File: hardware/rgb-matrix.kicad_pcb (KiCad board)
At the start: 4 copper layers, 58 x 58 mm, 138 parts, among them CON1 VEXT, P1 MATRIX_BOT, P10 PSOUTH, P11 PEAST, P12 WEST, P13 NORTH, P14 SOUTH, P15 EAST, P2 MATRIX_TOP, P3 SWD, P4 SPI3, P5 UART5, P6 VEXT, P7 USB_B, P8 PWEST, P9 PNORTH, SW1 RESET, SW2 BOOT, U1 74AC244, U2 74AC244, U3 74AC244, U4 ULN2803A, U5 STM32F405R, U6 LD3985M33R, U7 USBUF01W6, X1 8MHz

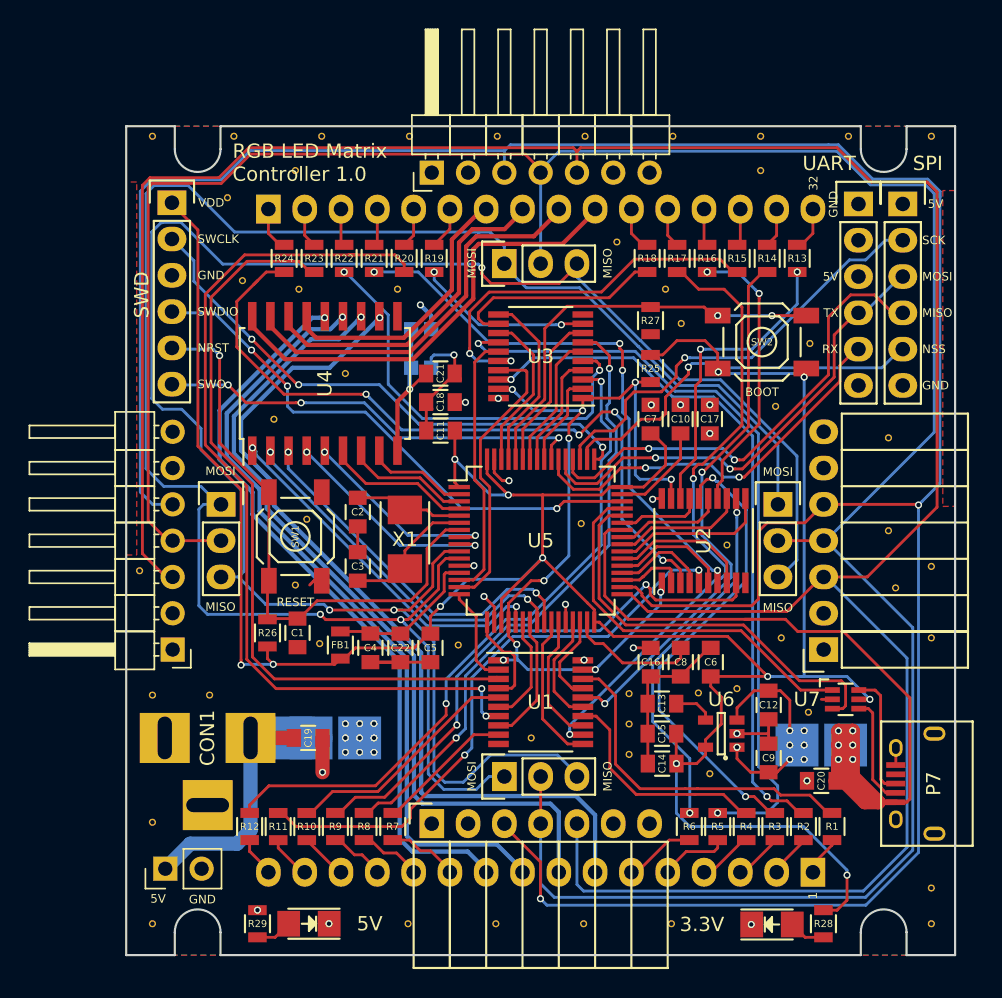
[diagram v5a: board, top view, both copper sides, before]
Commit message: Add silk: name and URL
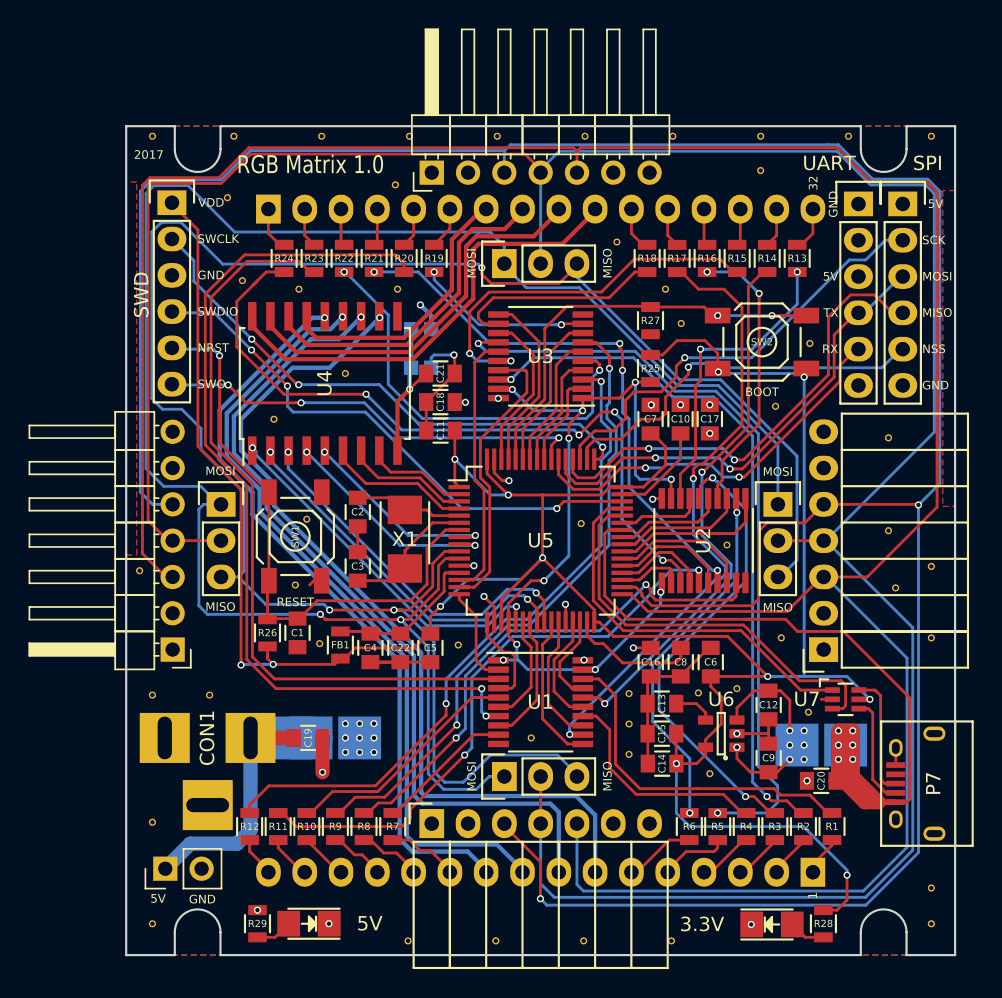
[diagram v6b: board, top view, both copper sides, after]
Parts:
- moved REF** 7.07 mm to (152.0, 76.3)
- moved REF** 1.20 mm to (152.9, 129.2)
- moved REF** 1.20 mm to (159.0, 129.2)
- moved REF** 1.20 mm to (165.2, 129.2)
- moved REF** 1.20 mm to (171.3, 129.2)
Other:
- board text added: "2017"
- board text added: "RGB Matrix 1.0"
- board text added: "https://github.com/joh/rgb-matrix"
- board text removed: "BOTTOM"
- board text removed: "RGB LED Matrix Controller 1.0"
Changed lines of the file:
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@@
     (area 133.088999 72.120999 191.239001 130.271001)
     (thickness 1.6)
-    (drawings 69)
+    (drawings 70)
     (tracks 1575)
     (zones 0)
@@
   )
   (module VIA-0.5mm (layer Top)
-    (at 152.885715 128 180)
+    (at 152.885715 129.2 180)
     (fp_text reference REF** (at 0 0.4 180) (layer F.SilkS) hide
       (effects (font (size 0.127 0.127) (thickness 0.03175)))
@@
   )
   (module VIA-0.5mm (layer Top)
-    (at 159.028572 128 180)
+    (at 159.028572 129.2 180)
     (fp_text reference REF** (at 0 0.4 180) (layer F.SilkS) hide
       (effects (font (size 0.127 0.127) (thickness 0.03175)))
@@
   )
   (module VIA-0.5mm (layer Top)
-    (at 165.171429 128 180)
+    (at 165.171429 129.2 180)
     (fp_text reference REF** (at 0 0.4 180) (layer F.SilkS) hide
       (effects (font (size 0.127 0.127) (thickness 0.03175)))
@@
   )
   (module VIA-0.5mm (layer Top)
-    (at 171.314286 128 180)
+    (at 171.314286 129.2 180)
     (fp_text reference REF** (at 0 0.4 180) (layer F.SilkS) hide
       (effects (font (size 0.127 0.127) (thickness 0.03175)))
@@
   )
   (module VIA-0.5mm (layer Top)
-    (at 145 75.3)
+    (at 152 76.3)
     (fp_text reference REF** (at 0 0.4) (layer F.SilkS) hide
       (effects (font (size 0.127 0.127) (thickness 0.03175)))
@@
     )
   )
-  (gr_text "RGB LED Matrix\nController 1.0" (at 140.6 74.75) (layer F.SilkS)
-    (effects (font (size 1 1) (thickness 0.15)) (justify left))
+  (gr_text https://github.com/joh/rgb-matrix (at 175.8 127.9) (layer B.SilkS)
+    (effects (font (size 1 1) (thickness 0.15)) (justify left mirror))
+  )
+  (gr_text 2017 (at 133.7 74.2) (layer F.SilkS)
+    (effects (font (size 0.6 0.6) (thickness 0.125)) (justify left))
+  )
+  (gr_text "RGB Matrix 1.0" (at 140.9 74.9) (layer F.SilkS)
+    (effects (font (size 1.25 1) (thickness 0.2)) (justify left))
   )
   (gr_text GND (at 185.392856 108.816) (layer B.SilkS)
@@
     (effects (font (size 1 1) (thickness 0.15)) (justify mirror))
   )
-  (gr_text BOTTOM (at 162.15 128) (layer B.SilkS)
-    (effects (font (size 1 1) (thickness 0.15)) (justify mirror))
-  )

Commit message: Add silk art, minor fixes
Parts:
- removed the REF** at (161.5, 115.0)
- added REF***: OSHW-Logo_5.7x6mm_SilkScreen, Symbols:OSHW-Logo_5.7x6mm_SilkScreen, B.Cu at (148.9, 102.0)
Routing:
- net GND: track 44.8 -> 55.9 mm, vias 13 -> 14
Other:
- board text added: "Jan 2017"
- board text removed: "2017"

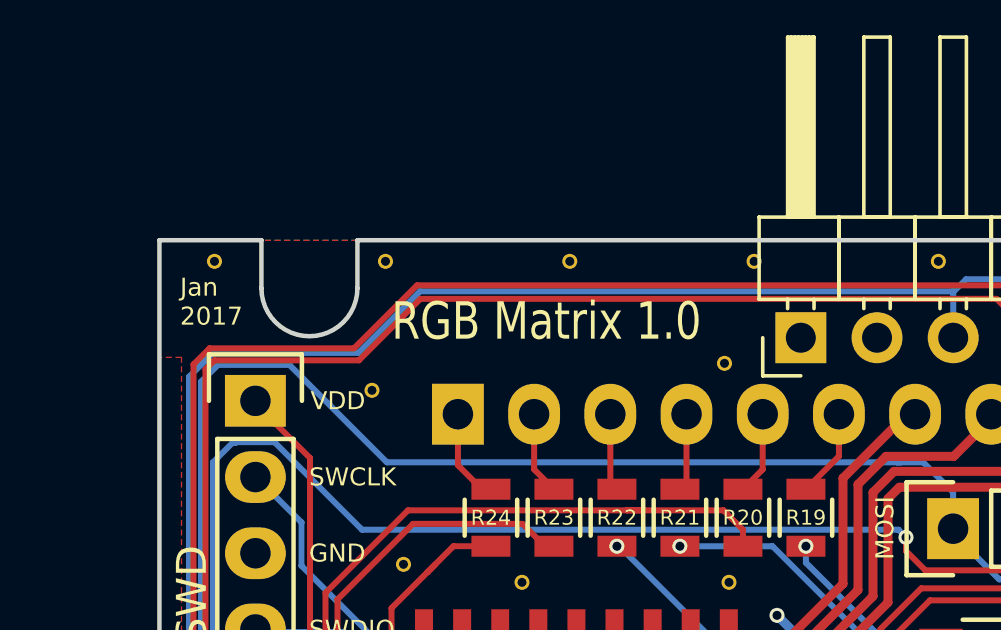
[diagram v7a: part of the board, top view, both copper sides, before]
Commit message: Fix solder mask clearance
Reduce clearance to 0.05mm so there is solder mask between all pads!
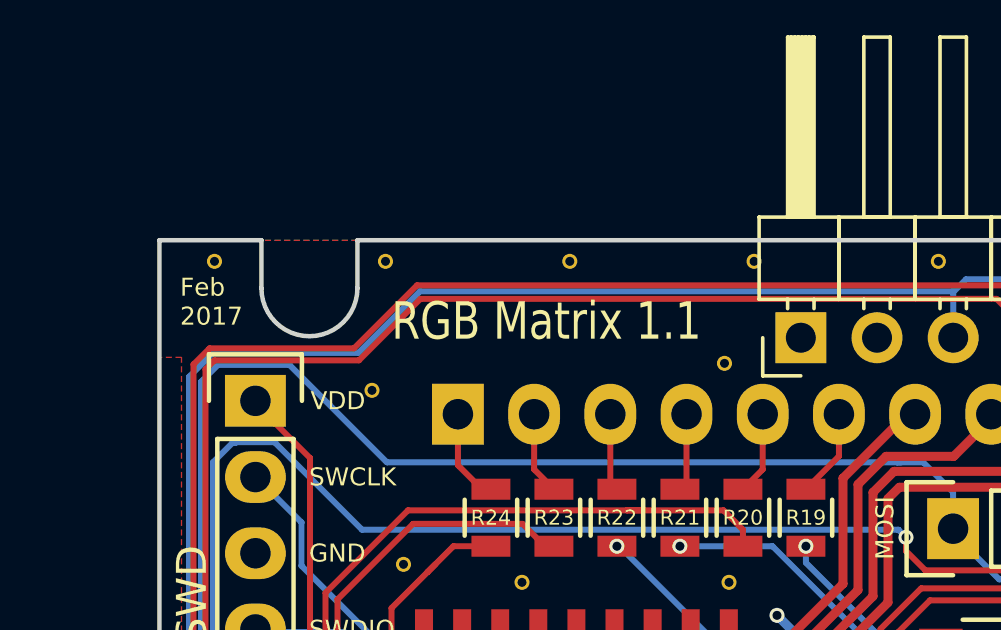
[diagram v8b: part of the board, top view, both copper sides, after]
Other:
- rule pad_to_mask_clearance: 0.2 -> 0.05
- board text added: "Feb 2017"
- board text added: "RGB Matrix 1.1"
- board text removed: "Jan 2017"
- board text removed: "RGB Matrix 1.0"
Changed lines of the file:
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@@
     (mod_text_size 1 1)
     (mod_text_width 0.15)
-    (pad_size 0.5 0.5)
-    (pad_drill 0.3)
-    (pad_to_mask_clearance 0.2)
+    (pad_size 3 3)
+    (pad_drill 0)
+    (pad_to_mask_clearance 0.05)
     (aux_axis_origin 0 0)
     (visible_elements FFFFFF7F)
@@
     )
   )
-  (module rgb-matrix:SMD-solder-bridge-1mm (layer Bottom)
-    (at 153.8 86.4)
-    (fp_text reference JP1 (at 3.75 0) (layer B.SilkS)
-      (effects (font (size 1 1) (thickness 0.15)) (justify mirror))
-    )
-    (fp_text value CA (at -3.5 0) (layer B.SilkS)
-      (effects (font (size 1 1) (thickness 0.15)) (justify mirror))
-    )
-    (fp_line (start 1.7 1) (end -1.7 1) (layer B.SilkS) (width 0.2))
-    (fp_line (start -1.7 1) (end -1.7 -1) (layer B.SilkS) (width 0.2))
-    (fp_line (start -1.7 -1) (end 1.7 -1) (layer B.SilkS) (width 0.2))
-    (fp_line (start 1.7 -1) (end 1.7 1) (layer B.SilkS) (width 0.2))
-    (pad 1 smd rect (at -0.7 0) (size 1 1) (layers Bottom B.Paste B.Mask)
-      (net 122 "Net-(C21-Pad1)"))
-    (pad 2 smd rect (at 0.7 0) (size 1 1) (layers Bottom B.Paste B.Mask)
-      (net 8 +5V))
-  )
-  (module rgb-matrix:SMD-solder-bridge-1mm (layer Bottom)
-    (at 153.8 89.1 180)
-    (fp_text reference JP2 (at -3.75 0 180) (layer B.SilkS)
-      (effects (font (size 1 1) (thickness 0.15)) (justify mirror))
-    )
-    (fp_text value CC (at 3.5 0 180) (layer B.SilkS)
-      (effects (font (size 1 1) (thickness 0.15)) (justify mirror))
-    )
-    (fp_line (start 1.7 1) (end -1.7 1) (layer B.SilkS) (width 0.2))
-    (fp_line (start -1.7 1) (end -1.7 -1) (layer B.SilkS) (width 0.2))
-    (fp_line (start -1.7 -1) (end 1.7 -1) (layer B.SilkS) (width 0.2))
-    (fp_line (start 1.7 -1) (end 1.7 1) (layer B.SilkS) (width 0.2))
-    (pad 1 smd rect (at -0.7 0 180) (size 1 1) (layers Bottom B.Paste B.Mask)
-      (net 1 GND))
-    (pad 2 smd rect (at 0.7 0 180) (size 1 1) (layers Bottom B.Paste B.Mask)
-      (net 122 "Net-(C21-Pad1)"))
-  )
-  (module rgb-matrix:SMD-solder-bridge-3mm (layer Bottom)
-    (at 147.8 115)
-    (fp_text reference JP3 (at 0.01 -3.5) (layer B.SilkS)
-      (effects (font (size 1 1) (thickness 0.15)) (justify mirror))
-    )
-    (fp_text value Vext (at 0 3.5) (layer B.SilkS)
-      (effects (font (size 1 1) (thickness 0.15)) (justify mirror))
-    )
-    (fp_line (start 3.7 2) (end -3.7 2) (layer B.SilkS) (width 0.2))
-    (fp_line (start -3.7 2) (end -3.7 -2) (layer B.SilkS) (width 0.2))
-    (fp_line (start -3.7 -2) (end 3.7 -2) (layer B.SilkS) (width 0.2))
-    (fp_line (start 3.7 -2) (end 3.7 2) (layer B.SilkS) (width 0.2))
-    (pad 1 smd rect (at -1.7 0) (size 3 3) (layers Bottom B.Paste B.Mask)
-      (net 118 /power/VEXT))
-    (pad 2 smd rect (at 1.7 0) (size 3 3) (layers Bottom B.Paste B.Mask)
-      (net 8 +5V))
-  )
-  (module rgb-matrix:SMD-solder-bridge-3mm (layer Bottom)
-    (at 181.8 115.5 180)
-    (fp_text reference JP4 (at 0 3.5 180) (layer B.SilkS)
-      (effects (font (size 1 1) (thickness 0.15)) (justify mirror))
-    )
-    (fp_text value Vbus (at 0 -3.5 180) (layer B.SilkS)
-      (effects (font (size 1 1) (thickness 0.15)) (justify mirror))
-    )
-    (fp_line (start 3.7 2) (end -3.7 2) (layer B.SilkS) (width 0.2))
-    (fp_line (start -3.7 2) (end -3.7 -2) (layer B.SilkS) (width 0.2))
-    (fp_line (start -3.7 -2) (end 3.7 -2) (layer B.SilkS) (width 0.2))
-    (fp_line (start 3.7 -2) (end 3.7 2) (layer B.SilkS) (width 0.2))
-    (pad 1 smd rect (at -1.7 0 180) (size 3 3) (layers Bottom B.Paste B.Mask)
-      (net 9 VBUS))
-    (pad 2 smd rect (at 1.7 0 180) (size 3 3) (layers Bottom B.Paste B.Mask)
-      (net 8 +5V))
-  )
   (module rgb-matrix:BARREL_JACK (layer Top)
     (at 135.66334 115)
@@
       (xy 0.376964 2.709982)) (layer B.SilkS) (width 0.01))
   )
+  (module rgb-matrix:SMD-solder-bridge-3mm (layer Bottom)
+    (at 147.8 115)
+    (fp_text reference JP3 (at 0 -3.1) (layer B.SilkS)
+      (effects (font (size 1 1) (thickness 0.15)) (justify mirror))
+    )
+    (fp_text value Vext (at 0 3.2) (layer B.SilkS)
+      (effects (font (size 1 1) (thickness 0.15)) (justify mirror))
+    )
+    (fp_line (start 3.7 2) (end -3.7 2) (layer B.SilkS) (width 0.2))
+    (fp_line (start -3.7 2) (end -3.7 -2) (layer B.SilkS) (width 0.2))
+    (fp_line (start -3.7 -2) (end 3.7 -2) (layer B.SilkS) (width 0.2))
+    (fp_line (start 3.7 -2) (end 3.7 2) (layer B.SilkS) (width 0.2))
+    (pad 1 smd rect (at -1.7 0) (size 3 3) (layers Bottom B.Paste B.Mask)
+      (net 118 /power/VEXT) (solder_mask_margin 0.2))
+    (pad 2 smd rect (at 1.7 0) (size 3 3) (layers Bottom B.Paste B.Mask)
+      (net 8 +5V) (solder_mask_margin 0.2))
+  )
+  (module rgb-matrix:SMD-solder-bridge-3mm (layer Bottom)
+    (at 181.8 115.5 180)
+    (fp_text reference JP4 (at 0.01 3.1 180) (layer B.SilkS)
+      (effects (font (size 1 1) (thickness 0.15)) (justify mirror))
+    )
+    (fp_text value Vbus (at 0 -3.2 180) (layer B.SilkS)
+      (effects (font (size 1 1) (thickness 0.15)) (justify mirror))
+    )
+    (fp_line (start 3.7 2) (end -3.7 2) (layer B.SilkS) (width 0.2))
+    (fp_line (start -3.7 2) (end -3.7 -2) (layer B.SilkS) (width 0.2))
+    (fp_line (start -3.7 -2) (end 3.7 -2) (layer B.SilkS) (width 0.2))
+    (fp_line (start 3.7 -2) (end 3.7 2) (layer B.SilkS) (width 0.2))
+    (pad 1 smd rect (at -1.7 0 180) (size 3 3) (layers Bottom B.Paste B.Mask)
+      (net 9 VBUS) (solder_mask_margin 0.2))
+    (pad 2 smd rect (at 1.7 0 180) (size 3 3) (layers Bottom B.Paste B.Mask)
+      (net 8 +5V) (solder_mask_margin 0.2))
+  )
+  (module rgb-matrix:SMD-solder-bridge-1mm (layer Bottom)
+    (at 153.8 86.4)
+    (fp_text reference JP1 (at 3.75 0) (layer B.SilkS)
+      (effects (font (size 1 1) (thickness 0.15)) (justify mirror))
+    )
+    (fp_text value CA (at -3.5 0) (layer B.SilkS)
+      (effects (font (size 1 1) (thickness 0.15)) (justify mirror))
+    )
+    (fp_line (start 1.7 1) (end -1.7 1) (layer B.SilkS) (width 0.2))
+    (fp_line (start -1.7 1) (end -1.7 -1) (layer B.SilkS) (width 0.2))
+    (fp_line (start -1.7 -1) (end 1.7 -1) (layer B.SilkS) (width 0.2))
+    (fp_line (start 1.7 -1) (end 1.7 1) (layer B.SilkS) (width 0.2))
+    (pad 1 smd rect (at -0.7 0) (size 1 1) (layers Bottom B.Paste B.Mask)
+      (net 122 "Net-(C21-Pad1)") (solder_mask_margin 0.2))
+    (pad 2 smd rect (at 0.7 0) (size 1 1) (layers Bottom B.Paste B.Mask)
+      (net 8 +5V) (solder_mask_margin 0.2))
+  )
+  (module rgb-matrix:SMD-solder-bridge-1mm (layer Bottom)
+    (at 153.8 89.1 180)
+    (fp_text reference JP2 (at -3.75 0 180) (layer B.SilkS)
+      (effects (font (size 1 1) (thickness 0.15)) (justify mirror))
+    )
+    (fp_text value CC (at 3.5 0 180) (layer B.SilkS)
+      (effects (font (size 1 1) (thickness 0.15)) (justify mirror))
+    )
+    (fp_line (start 1.7 1) (end -1.7 1) (layer B.SilkS) (width 0.2))
+    (fp_line (start -1.7 1) (end -1.7 -1) (layer B.SilkS) (width 0.2))
+    (fp_line (start -1.7 -1) (end 1.7 -1) (layer B.SilkS) (width 0.2))
+    (fp_line (start 1.7 -1) (end 1.7 1) (layer B.SilkS) (width 0.2))
+    (pad 1 smd rect (at -0.7 0 180) (size 1 1) (layers Bottom B.Paste B.Mask)
+      (net 1 GND) (solder_mask_margin 0.2))
+    (pad 2 smd rect (at 0.7 0 180) (size 1 1) (layers Bottom B.Paste B.Mask)
+      (net 122 "Net-(C21-Pad1)") (solder_mask_margin 0.2))
+  )
   (gr_text https://github.com/joh/rgb-matrix (at 175.8 127.9) (layer B.SilkS)
     (effects (font (size 1 1) (thickness 0.15)) (justify left mirror))
   )
-  (gr_text "Jan\n2017" (at 133.85 74.25) (layer F.SilkS)
+  (gr_text "Feb\n2017" (at 133.85 74.25) (layer F.SilkS)
     (effects (font (size 0.6 0.6) (thickness 0.125)) (justify left))
   )
-  (gr_text "RGB Matrix 1.0" (at 140.9 74.9) (layer F.SilkS)
+  (gr_text "RGB Matrix 1.1" (at 140.9 74.9) (layer F.SilkS)
     (effects (font (size 1.25 1) (thickness 0.2)) (justify left))
   )
